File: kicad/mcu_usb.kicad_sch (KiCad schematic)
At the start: 47 parts, among them J4 USB-A host, SW2 BOOT, SW3 RESET, U10 RP2354A, U11 SRV05-4, U12 SY6280AAC, U6 SRV05-4, Y1 12MHz

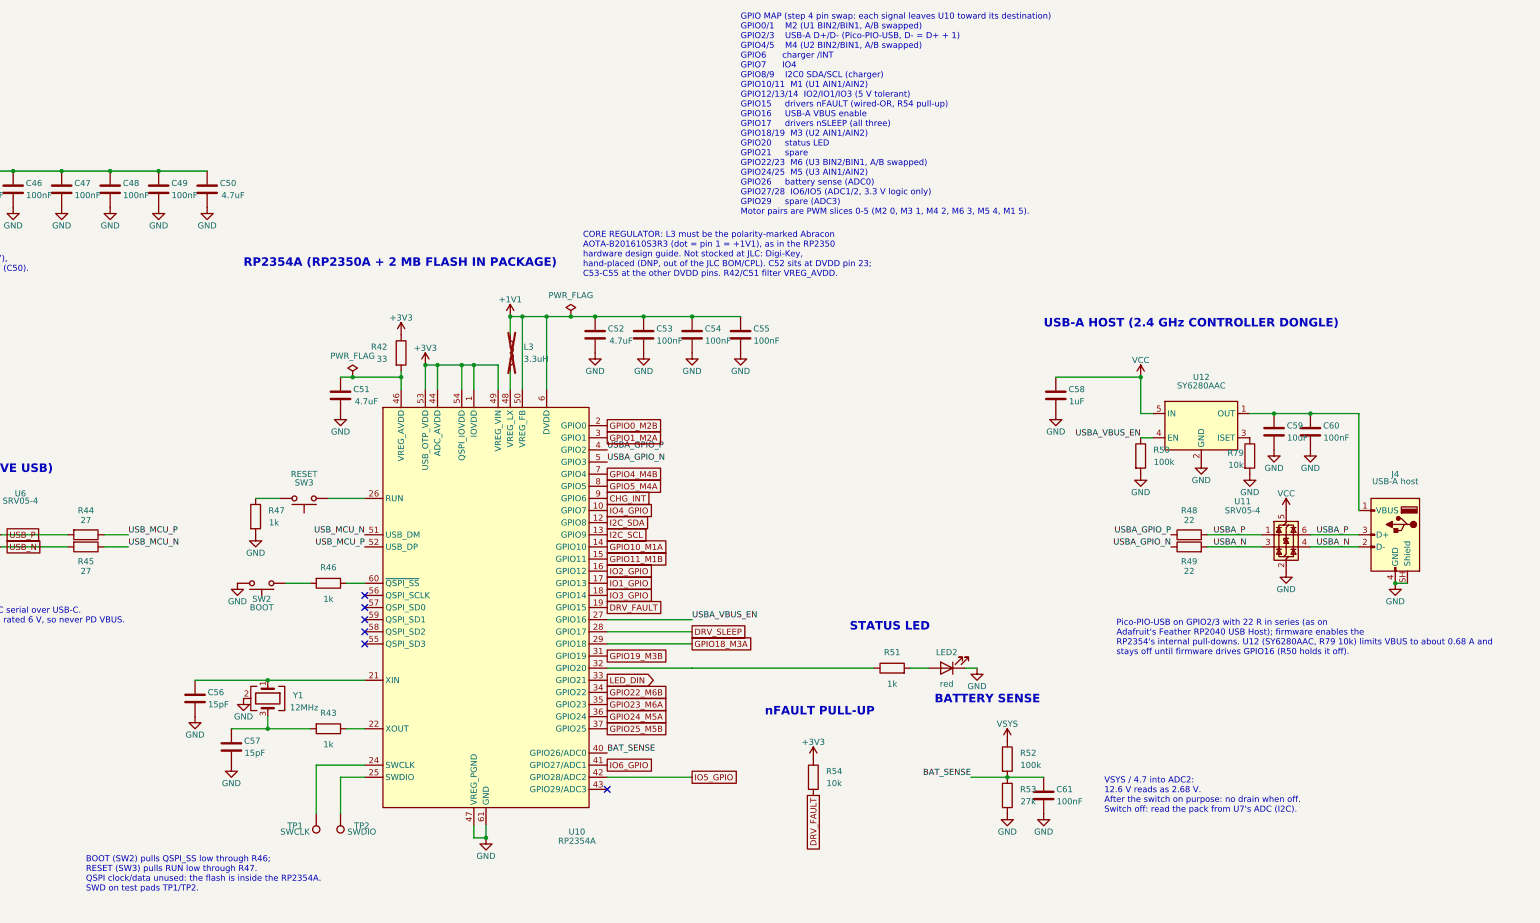
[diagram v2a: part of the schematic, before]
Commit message: Re-lay out rev 2 around an Ovonic 450 pack on top of the board
The internal pack is now an Ovonic 3S 450 mAh XT30 pack sitting 2 mm
above the board over the low-power logic area, on an XT30 pigtail. The
board is 88.5 x 47 mm with 2 mm corner radii, for a box of about
93.5 x 52 x 24.6 mm whose face has no openings.

- IO S1-S6 are a 3 x 6 right-angle header out of the left end, beside
  M5/M6, replacing the recessed vertical block.
- BOOT is a side-push switch on the top edge behind a pinhole sized for
  a 2.5 mm hex key; RESET is removed, with RUN on a bottom test pad
  beside SWCLK/SWDIO/GND.
- The CHG LED is a side-view part on the top edge; the GPIO status LED
  is removed now that the WS2812B stick shows status.
- The pack NTC is removed (a fixed 10k holds the charger's TS at 25 C);
  the protector's on-board TH1 stays.
- Q1, F1 and the other warm parts moved out from under the pack, and the
  GPIO map was re-swapped for the new placement (I2C on I2C1).

Schematic review passes; PCB review passes every gate except unrouted.

Co-Authored-By: Claude Opus 5.5 <noreply@anthropic.com>
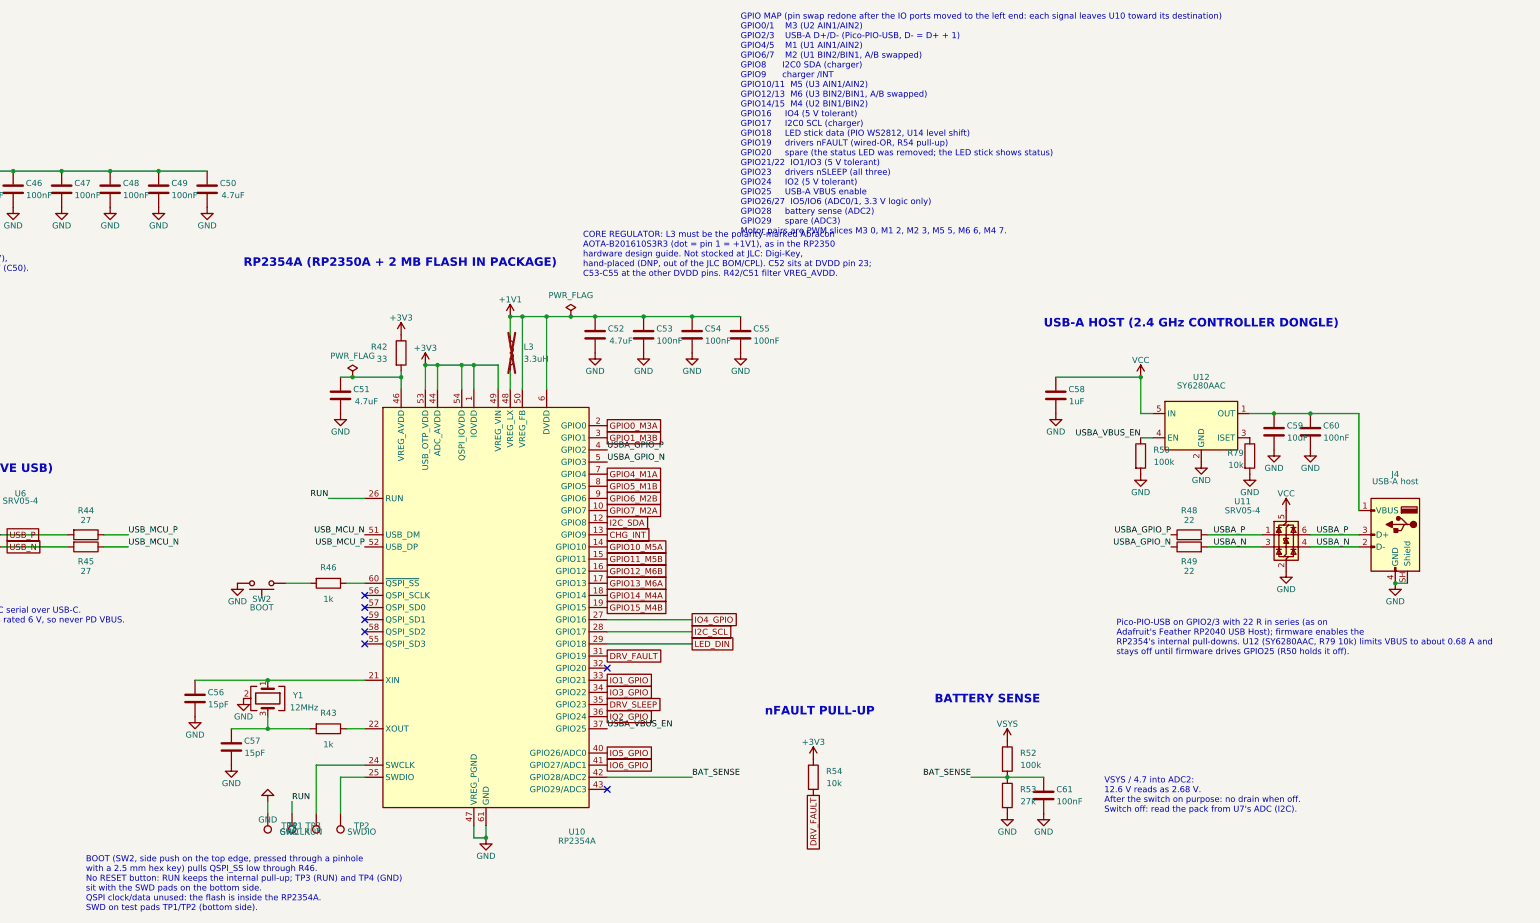
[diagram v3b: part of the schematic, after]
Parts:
- removed LED2: red, LED_SMD:LED_0603_1608Metric, symbol Device:LED
- removed R47, R51: 1k, Resistor_SMD:R_0402_1005Metric, symbol Device:R
- removed SW3: RESET, Button_Switch_SMD:SW_SPST_TS-1088-xR020, symbol Switch:SW_Push
- added TP3: RUN, TestPoint:TestPoint_Pad_D1.0mm, symbol Connector:TestPoint
- added TP4: GND, TestPoint:TestPoint_Pad_D1.0mm, symbol Connector:TestPoint
- SW2: footprint Button_Switch_SMD:SW_SPST_TS-1088-xR020 -> hexy:SW_Push_1P1T-MP_NO_Horizontal_Alps_SKRTLAE010_JLC; LCSC Part # C720477 -> C110293; MPN TS-1088-AR02016 -> SKRTLAE010; Manufacturer XUNPU -> ALPS Electric
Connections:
- net GPIO18_M3A is gone; now on net LED_DIN: U10.29 (GPIO18)
- net GPIO19_M3B is gone; now on net DRV_FAULT: U10.31 (GPIO19)
- net GPIO22_M6B is gone; now on net IO3_GPIO: U10.34 (GPIO22)
- net GPIO23_M6A is gone; now on net DRV_SLEEP: U10.35 (GPIO23)
- net GPIO24_M5A is gone; now on net IO2_GPIO: U10.36 (GPIO24)
- net GPIO25_M5B is gone; now on net USBA_VBUS_EN: U10.37 (GPIO25)
- net BAT_SENSE: now also U10.42 (GPIO28/ADC2); no longer U10.40 (GPIO26/ADC0)
- net CHG_INT: now also U10.13 (GPIO9); no longer U10.9 (GPIO6)
- net DRV_FAULT: no longer U10.19 (GPIO15)
- net DRV_SLEEP: no longer U10.28 (GPIO17)
- net GND: now also TP4.1
- net I2C_SCL: now also U10.28 (GPIO17); no longer U10.13 (GPIO9)
- net IO1_GPIO: now also U10.33 (GPIO21); no longer U10.17 (GPIO13)
- net IO2_GPIO: no longer U10.16 (GPIO12)
- net IO3_GPIO: no longer U10.18 (GPIO14)
- net IO4_GPIO: now also U10.27 (GPIO16); no longer U10.10 (GPIO7)
- net IO5_GPIO: now also U10.40 (GPIO26/ADC0); no longer U10.42 (GPIO28/ADC2)
- net LED_DIN: no longer U10.33 (GPIO21)
- net USBA_VBUS_EN: no longer U10.27 (GPIO16)
- net RUN: now reaches U10.26 (RUN)
- net RUN: now also TP3.1
- net GPIO0_M2B renamed GPIO0_M3A
- net GPIO10_M1A renamed GPIO10_M5A
- net GPIO11_M1B renamed GPIO11_M5B
- net GPIO1_M2A renamed GPIO1_M3B
- net GPIO4_M4B renamed GPIO4_M1A
- net GPIO5_M4A renamed GPIO5_M1B
- new net GPIO12_M6B: U10.16 (GPIO12)
- new net GPIO13_M6A: U10.17 (GPIO13)
- new net GPIO14_M4A: U10.18 (GPIO14)
- new net GPIO15_M4B: U10.19 (GPIO15)
- new net GPIO6_M2B: U10.9 (GPIO6)
- new net GPIO7_M2A: U10.10 (GPIO7)
- no-connect marks 6 -> 7
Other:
- note added: "BOOT (SW2, side push on the top edge, pressed through a pinhole with a 2.5 mm hex key) pulls QSPI_SS low through R46. No RESET button: RUN keeps the internal pull-up; TP3 (RUN) and TP4 (GND) sit with the SWD pads on the bottom side. QSPI clock/data unused: the flash is inside the RP2354A. SWD on test pads TP1/TP2 (bottom side)."
- note added: "GPIO MAP (pin swap redone after the IO ports moved to the left end: each signal leaves U10 toward its destination) GPIO0/1 M3 (U2 AIN1/AIN2) GPIO2/3 USB-A D+/D- (Pico-PIO-USB, D- = D+ + 1) GPIO4/5 M1 (U1 AIN1/AIN2) GPIO6/7 M2 (U1 BIN2/BIN1, A/B swapped) GPIO8 I2C0 SDA (charger) GPIO9 charger /INT GPIO10/11 M5 (U3 AIN1/AIN2) GPIO12/13 M6 (U3 BIN2/BIN1, A/B swapped) GPIO14/15 M4 (U2 BIN1/BIN2) GPIO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"
- note added: "Pico-PIO-USB on GPIO2/3 with 22 R in series (as on Adafruit's Feather RP2040 USB Host); firmware enables the RP2354's internal pull-downs. U12 (SY6280AAC, R79 10k) limits VBUS to about 0.68 A and stays off until firmware drives GPIO25 (R50 holds it off)."
- note removed: "BOOT (SW2) pulls QSPI_SS low through R46; RESET (SW3) pulls RUN low through R47. QSPI clock/data unused: the flash is inside the RP2354A. SWD on test pads TP1/TP2."
- note removed: "GPIO MAP (step 4 pin swap: each signal leaves U10 toward its destination) GPIO0/1 M2 (U1 BIN2/BIN1, A/B swapped) GPIO2/3 USB-A D+/D- (Pico-PIO-USB, D- = D+ + 1) GPIO4/5 M4 (U2 BIN2/BIN1, A/B swapped) GPIO6 charger /INT GPIO7 IO4 GPIO8/9 I2C0 SDA/SCL (charger) GPIO10/11 M1 (U1 AIN1/AIN2) GPIO12/13/14 IO2/IO1/IO3 (5 V tolerant) GPIO15 drivers nFAULT (wired-OR, R54 pull-up) GPIO16 USB-A VBUS enable 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"
- note removed: "Pico-PIO-USB on GPIO2/3 with 22 R in series (as on Adafruit's Feather RP2040 USB Host); firmware enables the RP2354's internal pull-downs. U12 (SY6280AAC, R79 10k) limits VBUS to about 0.68 A and stays off until firmware drives GPIO16 (R50 holds it off)."
- note removed: "STATUS LED"

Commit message: Fit the standard Ovonic 450 pack and recess the IO header
The earlier 50.5 x 25 x 14 mm pack size came from a mislabeled listing.
The layout now uses the standard Ovonic 80C 3S 450 mAh pack (design
envelope 46.5 x 25 x 21 mm) on top of the board, for a box of about
93.5 x 52 x 30 mm; the Long Size pack would have needed a ~110 mm box.

- S1-S6 (J5) move 5.55 mm inboard so the pin tips end 1 mm inside the
  left wall; the FET/shunt strip and nearby passives shift to suit.
- The pack carries a female XT30U-F, so J3 takes a male XT30U-M pigtail
  on 16 AWG. A vertical XT30UPB-M was checked and misses the 1 mm
  clearance under the face.
- IO1-IO4 GPIOs reordered for the new placement.

Schematic review passes; PCB review passes every gate except unrouted.

Co-Authored-By: Claude Opus 5.5 <noreply@anthropic.com>
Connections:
- net IO1_GPIO: now also U10.27 (GPIO16); no longer U10.33 (GPIO21)
- net IO2_GPIO: now also U10.33 (GPIO21); no longer U10.36 (GPIO24)
- net IO4_GPIO: now also U10.36 (GPIO24); no longer U10.27 (GPIO16)
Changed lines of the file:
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@@
 		)
 	)
-	(global_label "IO2_GPIO"
+	(global_label "IO4_GPIO"
 		(at 215.9 177.8 0)
 		(effects
@@
 		)
 	)
-	(global_label "IO4_GPIO"
+	(global_label "IO1_GPIO"
 		(at 233.68 157.48 0)
 		(effects
@@
 		)
 	)
-	(text "GPIO MAP (pin swap redone after the IO ports moved to the left end: each signal leaves U10 toward its destination)\nGPIO0/1    M3 (U2 AIN1/AIN2)\nGPIO2/3    USB-A D+/D- (Pico-PIO-USB, D- = D+ + 1)\nGPIO4/5    M1 (U1 AIN1/AIN2)\nGPIO6/7    M2 (U1 BIN2/BIN1, A/B swapped)\nGPIO8      I2C0 SDA (charger)\nGPIO9      charger /INT\nGPIO10/11  M5 (U3 AIN1/AIN2)\nGPIO12/13  M6 (U3 BIN2/BIN1, A/B swapped)\nGPIO14/15  M4 (U2 BIN1/BIN2)\nGPIO16     IO4 (5 V tolerant)\nGPIO17     I2C0 SCL (charger)\nGPIO18     LED stick data (PIO WS2812, U14 level shift)\nGPIO19     drivers nFAULT (wired-OR, R54 pull-up)\nGPIO20     spare (the status LED was removed; the LED stick shows status)\nGPIO21/22  IO1/IO3 (5 V tolerant)\nGPIO23     drivers nSLEEP (all three)\nGPIO24     IO2 (5 V tolerant)\nGPIO25     USB-A VBUS enable\nGPIO26/27  IO5/IO6 (ADC0/1, 3.3 V logic only)\nGPIO28     battery sense (ADC2)\nGPIO29     spare (ADC3)\nMotor pairs are PWM slices M3 0, M1 2, M2 3, M5 5, M6 6, M4 7."
+	(text "GPIO MAP (pin swap redone after the IO ports moved to the left end: each signal leaves U10 toward its destination)\nGPIO0/1    M3 (U2 AIN1/AIN2)\nGPIO2/3    USB-A D+/D- (Pico-PIO-USB, D- = D+ + 1)\nGPIO4/5    M1 (U1 AIN1/AIN2)\nGPIO6/7    M2 (U1 BIN2/BIN1, A/B swapped)\nGPIO8      I2C0 SDA (charger)\nGPIO9      charger /INT\nGPIO10/11  M5 (U3 AIN1/AIN2)\nGPIO12/13  M6 (U3 BIN2/BIN1, A/B swapped)\nGPIO14/15  M4 (U2 BIN1/BIN2)\nGPIO16     IO1 (5 V tolerant)\nGPIO17     I2C0 SCL (charger)\nGPIO18     LED stick data (PIO WS2812, U14 level shift)\nGPIO19     drivers nFAULT (wired-OR, R54 pull-up)\nGPIO20     spare (the status LED was removed; the LED stick shows status)\nGPIO21/22  IO2/IO3 (5 V tolerant)\nGPIO23     drivers nSLEEP (all three)\nGPIO24     IO4 (5 V tolerant)\nGPIO25     USB-A VBUS enable\nGPIO26/27  IO5/IO6 (ADC0/1, 3.3 V logic only)\nGPIO28     battery sense (ADC2)\nGPIO29     spare (ADC3)\nMotor pairs are PWM slices M3 0, M1 2, M2 3, M5 5, M6 6, M4 7."
 		(exclude_from_sim no)
 		(at 243.84 30.48 0)
@@
 		)
 	)
-	(global_label "IO1_GPIO"
+	(global_label "IO2_GPIO"
 		(at 215.9 170.18 0)
 		(effects

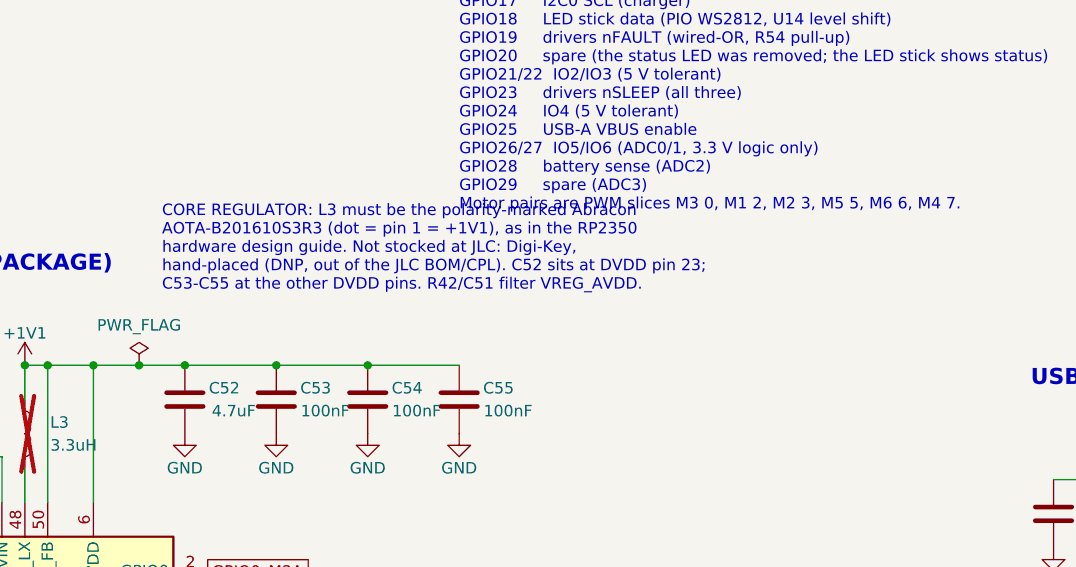
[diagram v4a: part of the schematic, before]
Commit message: Route rev 2 on a 6-layer board
Four layers couldn't route the fan-out around the RP2354A, so the board
moves to JLC's standard 1.6 mm 6-layer stack (JLC06161H-3313, ENIG,
via-in-pad): F signals, In1 GND, In2 signals, In3 power planes, In4 GND,
B signals. Placement is unchanged.

Review 53 passes every gate: nothing unrouted, 0 DRC errors. The critic
stopped at 3.9 after 10 iterations; the open findings are in
build/review/pcb/LOG.md, including DVDD pin 23's 100 nF (C54) sitting
about 11 mm of copper away.

Also adds the inner3/inner4 review views, the 6-layer quotes in
PARTS.md, and fixes the core-regulator note's cap names.

Co-Authored-By: Claude Opus 5.5 <noreply@anthropic.com>
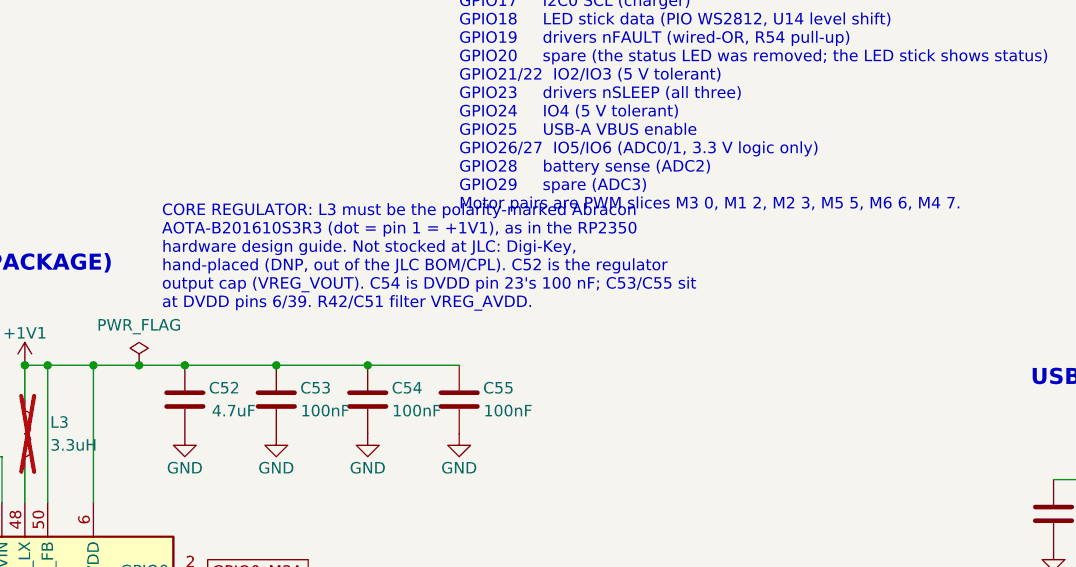
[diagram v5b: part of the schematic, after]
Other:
- note added: "CORE REGULATOR: L3 must be the polarity-marked Abracon AOTA-B201610S3R3 (dot = pin 1 = +1V1), as in the RP2350 hardware design guide. Not stocked at JLC: Digi-Key, hand-placed (DNP, out of the JLC BOM/CPL). C52 is the regulator output cap (VREG_VOUT). C54 is DVDD pin 23's 100 nF; C53/C55 sit at DVDD pins 6/39. R42/C51 filter VREG_AVDD."
- note removed: "CORE REGULATOR: L3 must be the polarity-marked Abracon AOTA-B201610S3R3 (dot = pin 1 = +1V1), as in the RP2350 hardware design guide. Not stocked at JLC: Digi-Key, hand-placed (DNP, out of the JLC BOM/CPL). C52 sits at DVDD pin 23; C53-C55 at the other DVDD pins. R42/C51 filter VREG_AVDD."
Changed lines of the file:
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@@
 		)
 	)
-	(text "CORE REGULATOR: L3 must be the polarity-marked Abracon\nAOTA-B201610S3R3 (dot = pin 1 = +1V1), as in the RP2350\nhardware design guide. Not stocked at JLC: Digi-Key,\nhand-placed (DNP, out of the JLC BOM/CPL). C52 sits at DVDD pin 23;\nC53-C55 at the other DVDD pins. R42/C51 filter VREG_AVDD."
+	(text "CORE REGULATOR: L3 must be the polarity-marked Abracon\nAOTA-B201610S3R3 (dot = pin 1 = +1V1), as in the RP2350\nhardware design guide. Not stocked at JLC: Digi-Key,\nhand-placed (DNP, out of the JLC BOM/CPL). C52 is the regulator\noutput cap (VREG_VOUT). C54 is DVDD pin 23's 100 nF; C53/C55 sit\nat DVDD pins 6/39. R42/C51 filter VREG_AVDD."
 		(exclude_from_sim no)
 		(at 210.82 76.2 0)
